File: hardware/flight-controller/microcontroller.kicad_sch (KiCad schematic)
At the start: 32 parts, among them J2 Conn_01x05, U4 ESP-12E, U5 STM32U535RET6, Y1 8MHz

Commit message: Mouser
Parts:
- SW2: value ~ -> KMS231GPLFS
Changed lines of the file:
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@@
 	(title_block
 		(title "UAV TVC Goose Flight Controller")
-		(date "2024-07-28")
+		(date "2024-07-31")
 		(rev "V2.1")
 		(comment 4 "Author: Eryk Możdżeń")
@@
 		(dnp no)
 		(property "Reference" "SW2"
-			(at 31.75 83.566 0)
+			(at 31.75 81.534 0)
 			(effects
 				(font
@@
 			)
 		)
-		(property "Value" "~"
+		(property "Value" "KMS231GPLFS"
 			(at 31.75 83.82 0)
 			(effects
@@
 			)
 		)
-		(property "Datasheet" ""
+		(property "Datasheet" "https://www.mouser.pl/datasheet/2/240/kms-3050656.pdf"
 			(at 31.75 83.82 0)
 			(effects

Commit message: routing: all signals routed
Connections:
- net ESP_RXD: now also U5.51 (PC10); no longer U5.53 (PC12)
- net ESP_TXD: now also U5.52 (PC11); no longer U5.54 (PD2)
- net GPS_RXD: now also U5.53 (PC12); no longer U5.51 (PC10)
- net GPS_TXD: now also U5.54 (PD2); no longer U5.52 (PC11)
- net IMU_INT: now also U5.50 (PA15); no longer U5.57 (PB5)
- net IMU_SCL: now also U5.61 (PB8); no longer U5.58 (PB6)
- net IMU_SDA: now also U5.62 (PB9); no longer U5.59 (PB7)
- net LED_R: now also U5.33 (PB12); no longer U5.26 (PB0)
- net MISC_SCL: now also U5.58 (PB6); no longer U5.61 (PB8)
- net MISC_SDA: now also U5.59 (PB7); no longer U5.62 (PB9)
- net PWR_INT: now also U5.57 (PB5); no longer U5.38 (PC7)
- net SERVO1: now also U5.43 (PA10); no longer U5.41 (PA8)
- net SERVO3: now also U5.41 (PA8); no longer U5.43 (PA10)
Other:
- moved on the sheet: R20, R21

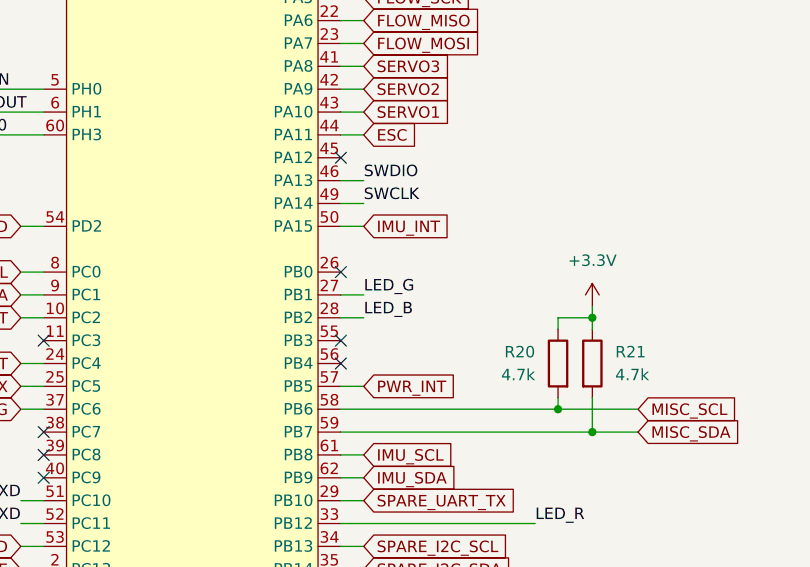
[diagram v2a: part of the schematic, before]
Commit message: fix IMU interrupt
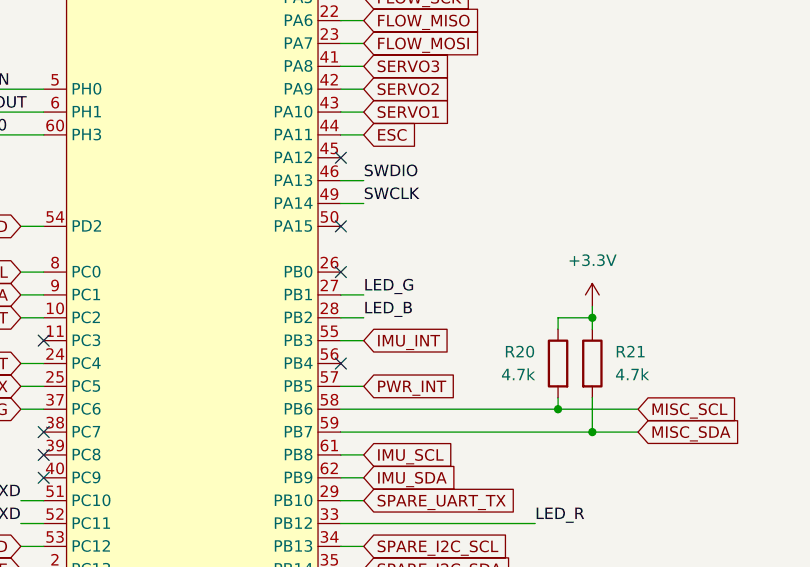
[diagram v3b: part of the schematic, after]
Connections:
- net IMU_INT: now also U5.55 (PB3); no longer U5.50 (PA15)
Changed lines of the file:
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@@
 	(title_block
 		(title "UAV TVC Goose Flight Controller")
-		(date "2024-08-04")
+		(date "2024-08-05")
 		(rev "V2.1")
 		(comment 4 "Author: Eryk Możdżeń")
@@
 	)
 	(no_connect
+		(at 110.49 127)
+	)
+	(no_connect
 		(at 110.49 119.38)
 	)
@@
 	)
 	(no_connect
-		(at 110.49 139.7)
-	)
-	(no_connect
 		(at 214.63 95.25)
 	)
@@
 	(wire
 		(pts
-			(xy 113.03 127) (xy 110.49 127)
-		)
-		(stroke
-			(width 0)
-			(type default)
-		)
-	)
-	(wire
-		(pts
 			(xy 138.43 137.16) (xy 138.43 138.43)
 		)
@@
 		(pts
 			(xy 245.11 72.39) (xy 260.35 72.39)
+		)
+		(stroke
+			(width 0)
+			(type default)
+		)
+	)
+	(wire
+		(pts
+			(xy 113.03 139.7) (xy 110.49 139.7)
 		)
 		(stroke
@@
 	(global_label "IMU_INT"
 		(shape input)
-		(at 113.03 127 0)
+		(at 113.03 139.7 0)
 		(fields_autoplaced yes)
 		(effects
@@
 		)
 		(property "Intersheetrefs" "${INTERSHEET_REFS}"
-			(at 123.2724 127 0)
+			(at 123.2724 139.7 0)
 			(effects
 				(font

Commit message: generate schematic in pdf
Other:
- title: UAV TVC Goose Flight Controller -> UAV TVC Goose II: Flight Controller
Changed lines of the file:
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@@
 	(paper "A4")
 	(title_block
-		(title "UAV TVC Goose Flight Controller")
+		(title "UAV TVC Goose II: Flight Controller")
 		(date "2024-08-05")
 		(rev "V2.1")
